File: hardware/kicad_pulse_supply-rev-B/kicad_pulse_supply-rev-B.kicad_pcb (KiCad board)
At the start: 4 copper layers, 127 x 96.5 mm, 181 parts, among them J1 USB_B_Micro, J2 SIG_EXT, J3 OPT_PWR, Q1 MMBT2222*, Q2 MMBT2222*, Q3 GAN7R0-150LBE, SW1 KMR211GLFS, U1 AP2112K-3.3, U10 LTC6244CMS8, U11 LTC6244CMS8, U12 TPS552892RYQR, U2 ESP32-WROOM-32D, U3 CP2104, U4 MAX4378, U5 UCC27611DRVT, U6 MCP1703T-5002E/MB, U7 LTC6244CMS8, U8 LTC6244CMS8, U9 LTC6244CMS8

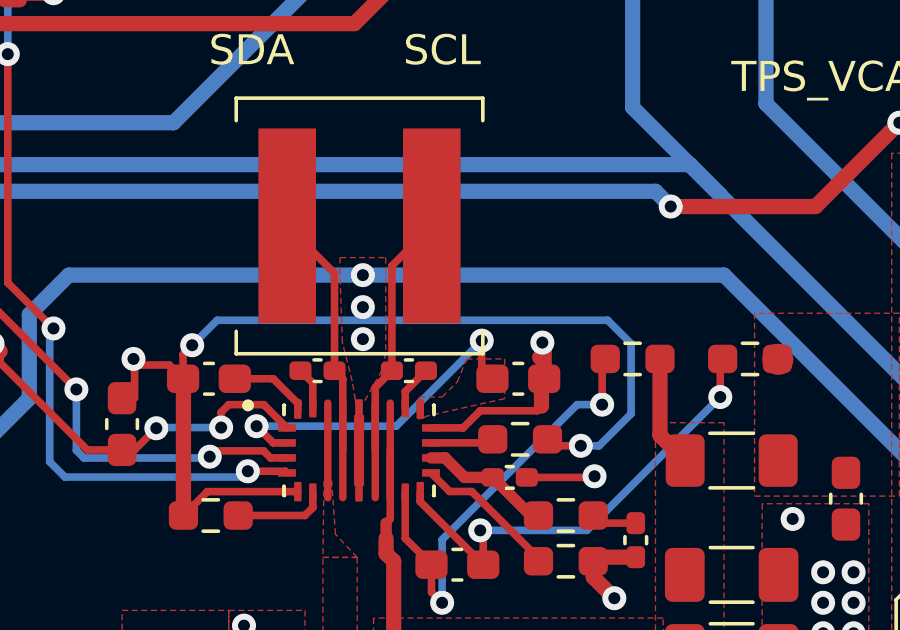
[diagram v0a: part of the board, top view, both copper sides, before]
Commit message: Board bringup: added TPS commands
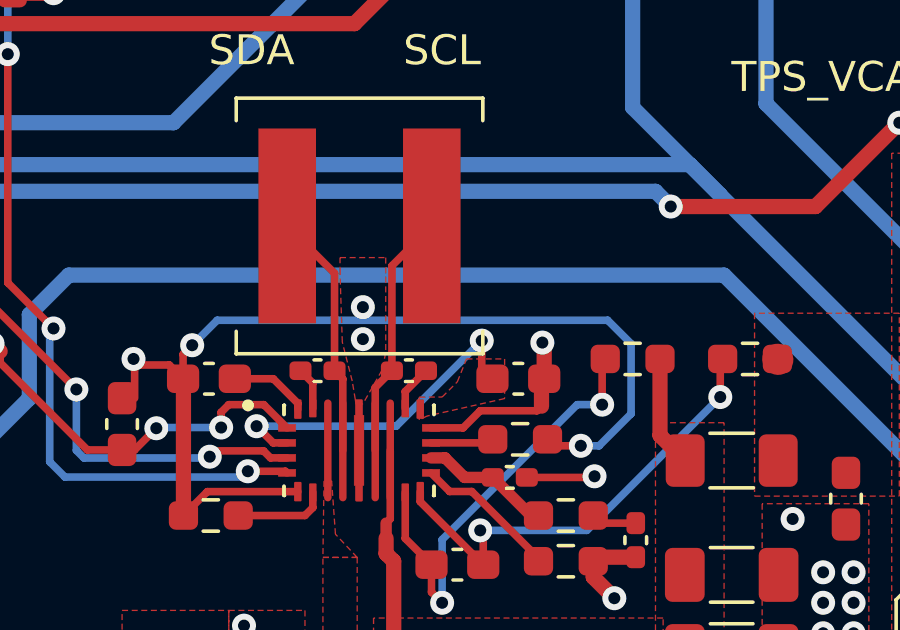
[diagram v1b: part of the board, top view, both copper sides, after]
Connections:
- C33 pad 1: GND -> ADC_10A
- R37 pad 2: GND -> ADC_10A
- TP20 pad 1: GND -> ADC_10A
- U2 pad 8: GND -> ADC_10A
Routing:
- net GND: track 275.9 -> 137.9 mm, vias 145 -> 142
- net ADC_10A: track 0.00 -> 137.9 mm, vias 0 -> 2
